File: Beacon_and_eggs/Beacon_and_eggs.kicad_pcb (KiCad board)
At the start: 4 copper layers, 40 x 80 mm, 73 parts, among them J1 USB_C_Receptacle_USB2.0_16P, J2 Conn_01x03_Pin, J3 Conn_01x02_Pin, Q1 NTA4151P, Q2 NTA4153N, U1 SA868S, U2 STM32F411CEU6TR, U3 ADXL343, U4 MIC5528-3.3YMX-TR, U6 BQ24070RHLR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

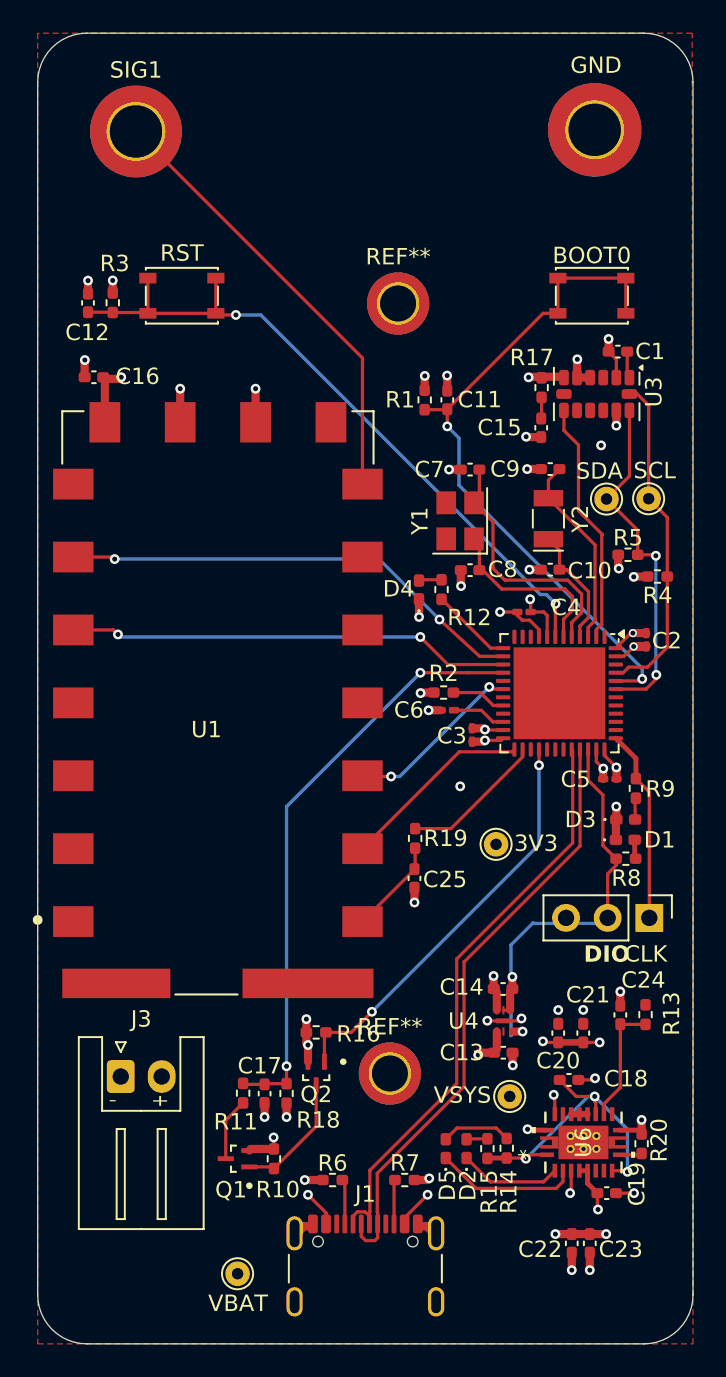
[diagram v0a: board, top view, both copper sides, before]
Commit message: reduce drc error to 0, updated step file
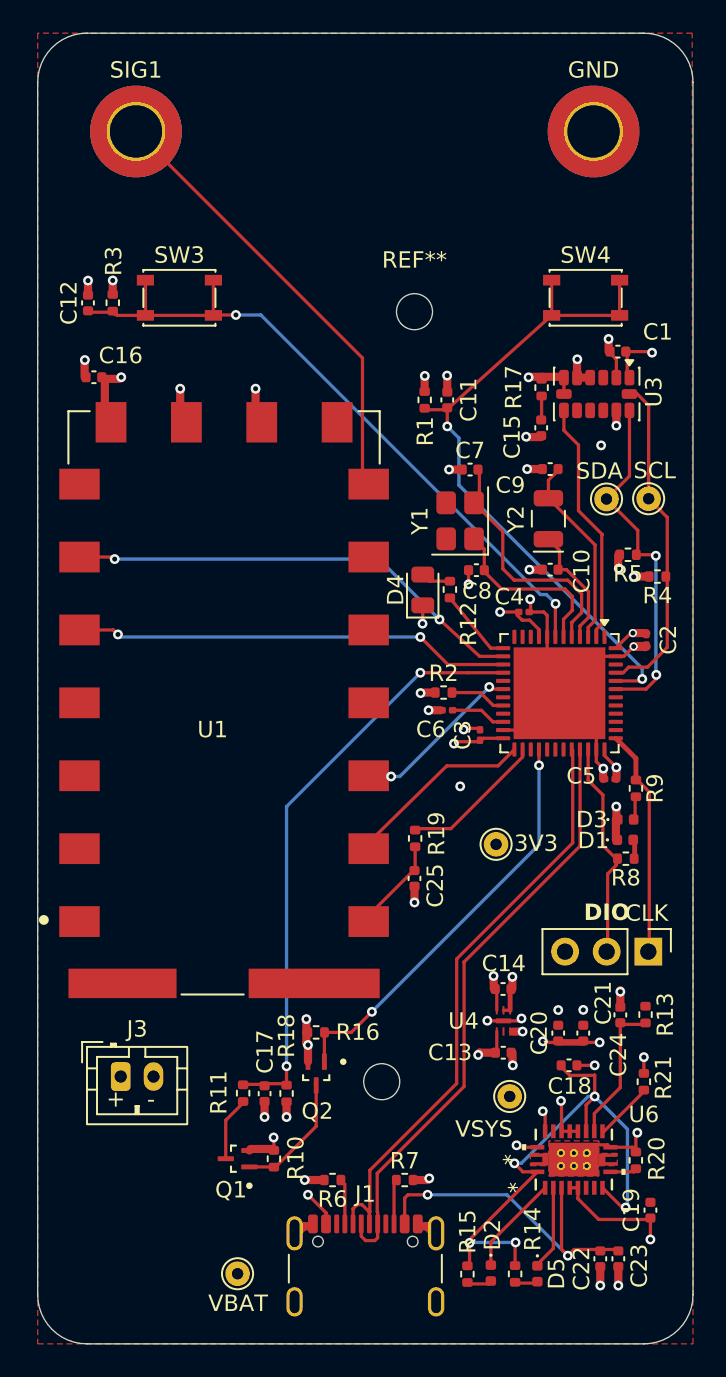
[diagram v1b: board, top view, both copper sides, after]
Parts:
- removed BOOT0: BOOT0, Button_Switch_SMD:SW_SPST_PTS810
- removed the GND at (154.0, 55.9)
- removed the REF** at (142.0, 66.5)
- removed the REF** at (141.5, 113.5)
- removed RST: RESET, Button_Switch_SMD:SW_SPST_PTS810
- added ?: , , F.Cu at (141.0, 114.0)
- added GND: , MountingHole:MountingHole_3.2mm_M3_DIN965_Pad_TopBottom, F.Cu at (153.9, 56.0)
- added R21: 10k, Resistor_SMD:R_0402_1005Metric, F.Cu at (157.0, 114.0)
- added REF**: MountingHole_2.2mm_M2, MountingHole:MountingHole_2.2mm_M2, F.Cu at (143.0, 67.0)
- added SW3: RESET, Button_Switch_SMD:SW_SPST_PTS810, F.Cu at (128.7, 66.2)
- added SW4: BOOT0, Button_Switch_SMD:SW_SPST_PTS810, F.Cu at (153.4, 66.2)
- C1, C10, C11, C12, C13, C14, C15, C16, C17, C18, C19, C20, C21, C22, C23, C24, C25, C7, C8, C9: footprint Capacitor_SMD:C_0402_1005Metric_Pad0.74x0.62mm_HandSolder -> Capacitor_SMD:C_0402_1005Metric
- C2, C3, C4, C5, C6: footprint Capacitor_SMD:C_0201_0603Metric_Pad0.64x0.40mm_HandSolder -> Capacitor_SMD:C_0201_0603Metric
- D1, D3: footprint Diode_SMD:D_0402_1005Metric_Pad0.77x0.64mm_HandSolder -> Diode_SMD:D_0402_1005Metric
- D2, D5: footprint LED_SMD:LED_0402_1005Metric_Pad0.77x0.64mm_HandSolder -> LED_SMD:LED_0402_1005Metric
- D4: footprint LED_SMD:LED_0402_1005Metric_Pad0.77x0.64mm_HandSolder -> LED_SMD:LED_0805_2012Metric
- J3: footprint Connector_JST:JST_XH_S2B-XH-A_1x02_P2.50mm_Horizontal -> Connector_JST:JST_PH_B2B-PH-K_1x02_P2.00mm_Vertical
- R1, R10, R11, R12, R13, R14, R15, R16, R17, R18, R19, R2, R20, R3, R4, R5, R6, R7, R8, R9: footprint Resistor_SMD:R_0402_1005Metric_Pad0.72x0.64mm_HandSolder -> Resistor_SMD:R_0402_1005Metric
- moved D5 9.46 mm to (150.5, 125.7), turned to -90 degrees
- moved R15 7.76 mm to (146.2, 125.7), turned to -90 degrees
- moved D2 7.73 mm to (147.7, 125.7), turned to -90 degrees
- moved R14 7.69 mm to (149.1, 125.7), turned to -90 degrees
- moved C19 2.86 mm to (157.4, 121.8), turned to 90 degrees
- moved J2 2.06 mm to (157.3, 106.1)
- moved C22 1.98 mm to (154.3, 124.8)
- moved C23 1.98 mm to (155.4, 124.8)
- moved U6 1.20 mm to (152.7, 118.8)
- moved R20 1.08 mm to (156.5, 118.8)
- moved C18 0.89 mm to (152.4, 113.0)
- moved R12 0.51 mm to (145.2, 84.0)
- moved C3 0.48 mm to (147.0, 92.8)
- moved C8 0.39 mm to (146.8, 82.8)
- moved U1 0.38 mm to (131.4, 90.9)
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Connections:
- C1 pad 1: Net-(U3-Vdd_I/O) -> +3.3V
- U3 pad 1: Net-(U3-Vdd_I/O) -> +3.3V
- U3 pad 7: unconnected-(U3-~{CS}-Pad7) -> +3.3V
- U6 pad 12: unconnected-(U6-TS-Pad12) -> Net-(U6-TS)
- U6 pad 21: unconnected-(U6-EPAD-Pad21) -> GND
- U6 pad V: (no net) -> GND
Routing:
- net /VREF: track 19.8 -> 35.4 mm, vias 3 -> 5
- net VBUS: track 9.37 -> 23.6 mm, vias 5 -> 3
- net GND: track 67.5 -> 74.3 mm
- net +3.3V: track 18.0 -> 23.2 mm, vias 10 -> 11
- net VBAT: track 5.38 -> 9.59 mm
- net Net-(D5-K): track 8.76 -> 5.08 mm
- net Net-(U6-TS): track 0.00 -> 3.53 mm
- net Net-(D5-A): track 4.27 -> 1.38 mm
- net /SWDIO: track 11.2 -> 13.3 mm
- net /SWCLK: track 12.0 -> 14.1 mm
- net VSYS: track 11.2 -> 13.1 mm, vias 5 -> 6
- net /USB_DN: track 37.0 -> 38.8 mm
- net Net-(U3-Vdd_I/O): track 1.64 -> 0.00 mm
- net Net-(U6-DPPM): track 7.45 -> 8.73 mm
- net /BOOT0: track 42.2 -> 41.6 mm

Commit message: changed batery connector footprint from vert. to horz.
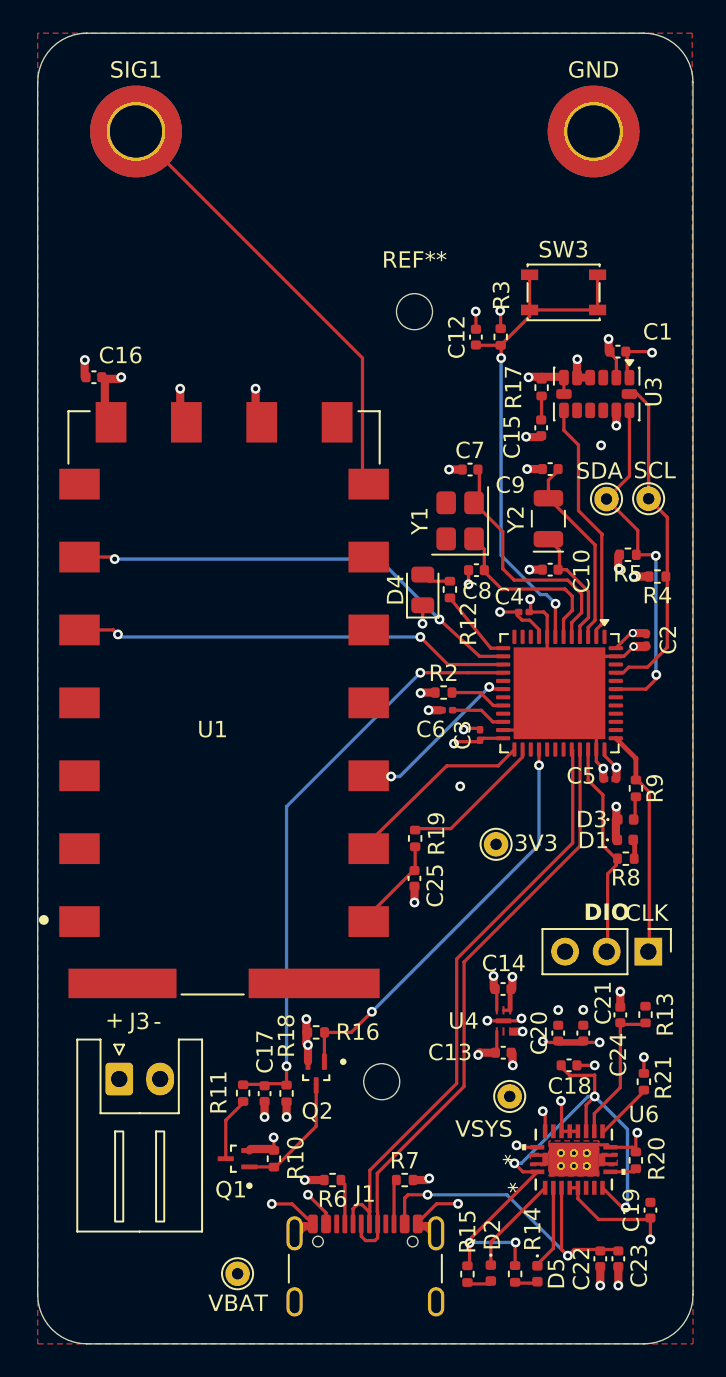
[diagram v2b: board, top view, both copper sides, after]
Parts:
- removed C11: 0.1uF, Capacitor_SMD:C_0402_1005Metric
- removed R1: 10k, Resistor_SMD:R_0402_1005Metric
- removed SW4: BOOT0, Button_Switch_SMD:SW_SPST_PTS810
- J3: footprint Connector_JST:JST_PH_B2B-PH-K_1x02_P2.00mm_Vertical -> Connector_JST:JST_XH_S2B-XH-A_1x02_P2.50mm_Horizontal
- moved C12 23.8 mm to (146.8, 68.5)
- moved R3 23.8 mm to (148.3, 68.5)
- moved SW3 23.5 mm to (152.1, 65.8)
- moved J3 0.18 mm to (125.0, 113.8)
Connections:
- U2 pad 44: /BOOT0 -> unconnected-(U2-BOOT0-Pad44)
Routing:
- net /BOOT0: track 41.6 -> 0.00 mm, vias 2 -> 0
- net /NRST: track 42.5 -> 32.3 mm
- net GND: track 74.3 -> 78.7 mm

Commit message: updated step file, added 3D components
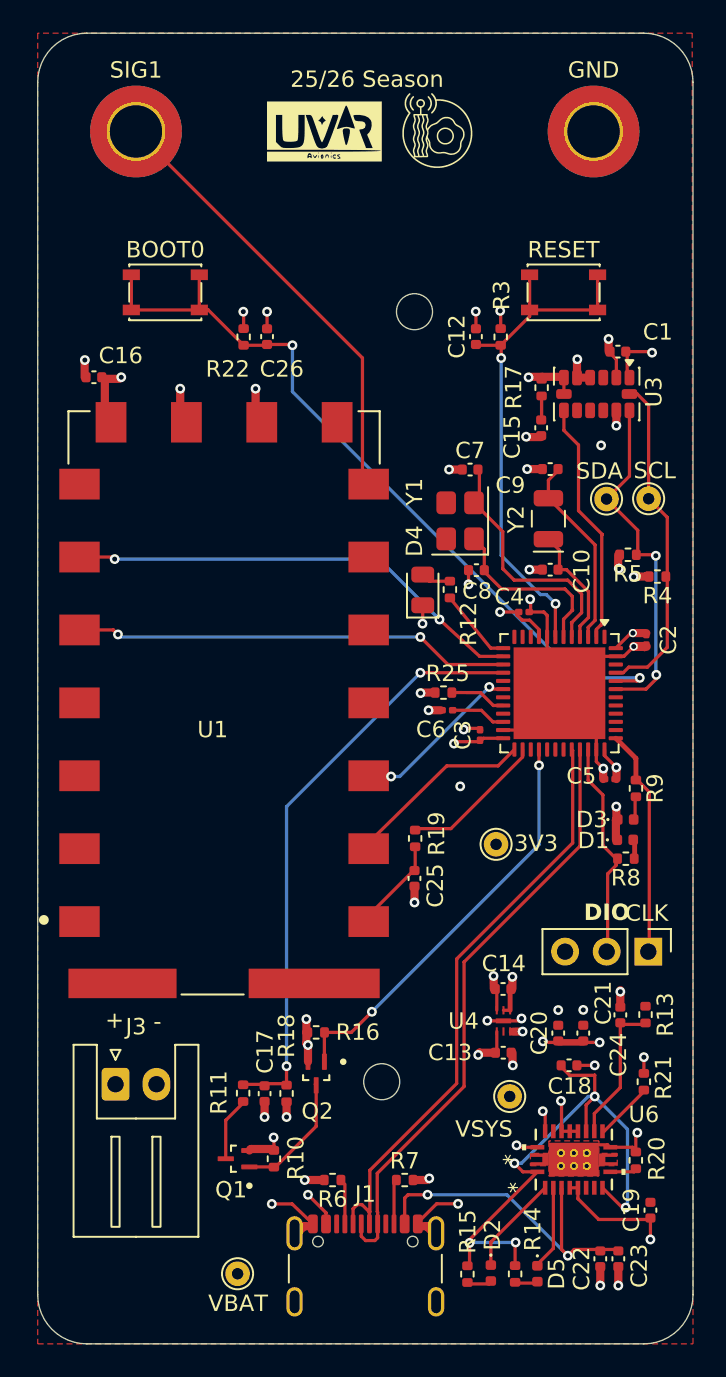
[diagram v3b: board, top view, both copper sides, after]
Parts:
- removed R2: 10k, Resistor_SMD:R_0402_1005Metric
- added BOOT0: BOOT0, Button_Switch_SMD:SW_SPST_PTS810, F.Cu at (127.8, 65.8)
- added C26: 0.1uF, Capacitor_SMD:C_0402_1005Metric, F.Cu at (134.0, 68.5)
- added G***: LOGO, Footprint Images:uvr_logo_3, F.Cu at (137.5, 56.0)
- added G***: LOGO, Footprint Images:beacon_and_eggs_logo_3, F.Cu at (144.4, 56.0)
- added R22: 10k, Resistor_SMD:R_0402_1005Metric, F.Cu at (132.6, 68.5)
- added R25: 10K, Resistor_SMD:R_0402_1005Metric, F.Cu at (144.8, 90.2)
- moved J3 0.39 mm to (124.8, 114.2)
- renumbered SW3 to RESET
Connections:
- U2 pad 44: unconnected-(U2-BOOT0-Pad44) -> /BOOT0
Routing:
- net /BOOT0: track 0.00 -> 47.9 mm, vias 0 -> 2
- net GND: track 78.7 -> 80.7 mm, vias 44 -> 46
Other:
- board text added: "25/26 Season"

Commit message: changed UART software  pins to hardware pins, fixed I2C pins
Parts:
- removed GND: , MountingHole:MountingHole_3.2mm_M3_DIN965_Pad_TopBottom
- removed SIG1: FABRIC_ANT_HOLES, MountingHole:MountingHole_3.2mm_M3_DIN965_Pad_TopBottom
- added ANT.GND1: Conn_01x01_Pin, MountingHole:MountingHole_3.2mm_M3_DIN965_Pad_TopBottom, F.Cu at (154.0, 56.0)
- added ANT.SIG1: Conn_01x01_Pin, MountingHole:MountingHole_3.2mm_M3_DIN965_Pad_TopBottom, F.Cu at (126.0, 56.0)
- moved C25 2.53 mm to (143.9, 99.2)
- moved R19 2.38 mm to (144.4, 97.2), turned to 180 degrees
- renumbered RESET to SW3, BOOT0 to SW4
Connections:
- U1 pad 16: /RXD -> /TXD
- U1 pad 17: /TXD -> /RXD
- U2 pad 18: /RXD -> unconnected-(U2-PB0-Pad18)
- U2 pad 25: /TXD -> unconnected-(U2-PB12-Pad25)
- U2 pad 30: unconnected-(U2-PA9-Pad30) -> /TXD
- U2 pad 31: unconnected-(U2-PA10-Pad31) -> /RXD
- U2 pad 42: unconnected-(U2-PB6-Pad42) -> /SCL
- U2 pad 45: /SCL -> unconnected-(U2-PB8-Pad45)
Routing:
- net /RXD: track 10.9 -> 15.4 mm
- net Net-(U1-MIC_IN): track 5.81 -> 8.56 mm
- net /TX_AUDIO_SIGNAL: track 8.82 -> 6.84 mm
- net /SCL: track 20.5 -> 22.2 mm
- net /TXD: track 11.8 -> 13.2 mm, vias 0 -> 2
- net unconnected-(U2-PB0-Pad18): track 0.00 -> 0.90 mm
- net GND: vias 46 -> 45

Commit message: labelled switches
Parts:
- renumbered SW4 to BOOT0, SW3 to RESET
